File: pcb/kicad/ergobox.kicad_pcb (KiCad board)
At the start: 2 copper layers, 234.6 x 150.2 mm, 80 parts, among them SW1 SW_Push, SW10 Kailh, SW11 Kailh, SW12 Kailh, SW13 Kailh, SW14 Kailh, SW15 Kailh, SW16 Kailh, SW17 Kailh, SW18 Kailh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

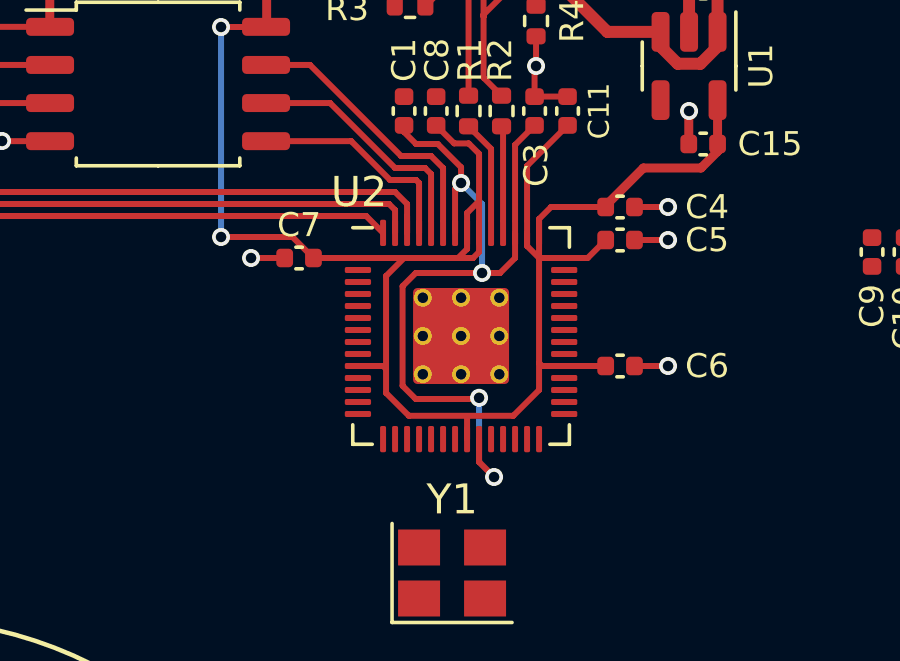
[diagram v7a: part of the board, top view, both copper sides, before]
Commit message: feat: adds +3V3 copper fill in RP2040 footprint
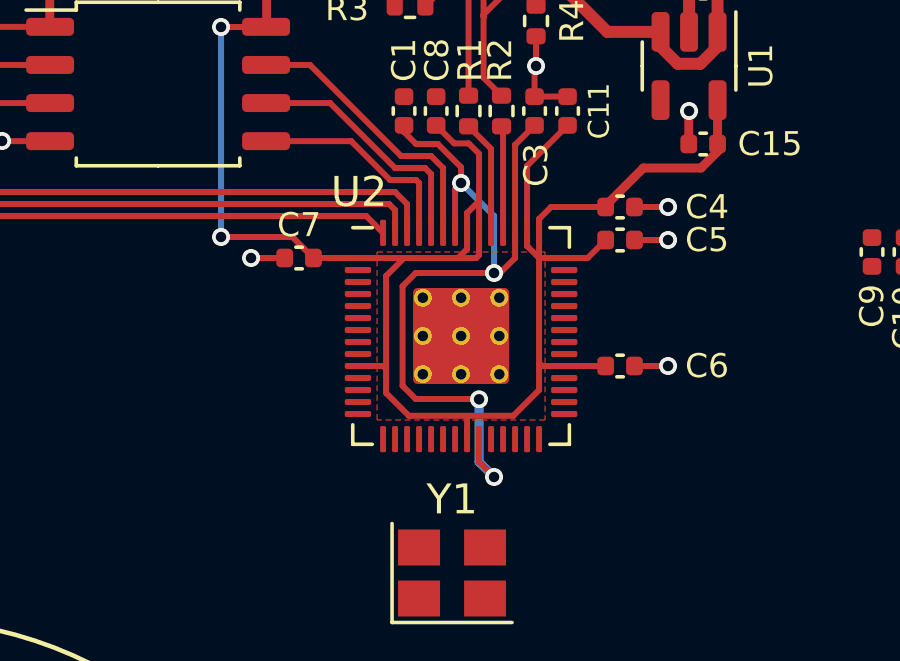
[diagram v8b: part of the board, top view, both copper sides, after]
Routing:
- added copper zone on F.Cu, net +3V3
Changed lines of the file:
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@@
   (segment (start 59.824314 27.2) (end 59.1 27.2) (width 0.2) (layer "F.Cu") (net 1))
   (segment (start 63.05 26.58) (end 62.4 27.23) (width 0.2) (layer "F.Cu") (net 1))
+  (segment (start 61.9 31.5) (end 62.4 31) (width 0.2) (layer "F.Cu") (net 1))
+  (segment (start 58.65 31.939379) (end 58.65 35.260621) (width 0.2) (layer "F.Cu") (net 1))
   (segment (start 60.6005 28.5) (end 60.6005 27.976186) (width 0.2) (layer "F.Cu") (net 1))
-  (segment (start 58.65 35.260621) (end 58.65 31.939379) (width 0.2) (layer "F.Cu") (net 1))
-  (segment (start 61.9 31.5) (end 61.3 31.5) (width 0.2) (layer "F.Cu") (net 1))
+  (segment (start 58.65 35.260621) (end 59.089379 35.7) (width 0.2) (layer "F.Cu") (net 1))
+  (segment (start 61.7 31.5) (end 61.9 31.5) (width 0.2) (layer "F.Cu") (net 1))
+  (segment (start 62.4 31) (end 62.4 30.1625) (width 0.2) (layer "F.Cu") (net 1))
   (segment (start 61.2 37.8) (end 61.7 38.3) (width 0.2) (layer "F.Cu") (net 1))
+  (segment (start 61.7 31.5) (end 59.089379 31.5) (width 0.2) (layer "F.Cu") (net 1))
   (segment (start 61.2 37.0375) (end 61.2 37.8) (width 0.2) (layer "F.Cu") (net 1))
-  (segment (start 62.4 31) (end 61.9 31.5) (width 0.2) (layer "F.Cu") (net 1))
+  (segment (start 59.089379 31.5) (end 58.65 31.939379) (width 0.2) (layer "F.Cu") (net 1))
   (segment (start 59.1 27.2) (end 58.7 26.8) (width 0.2) (layer "F.Cu") (net 1))
   (segment (start 60.6005 27.976186) (end 59.824314 27.2) (width 0.2) (layer "F.Cu") (net 1))
-  (segment (start 58.65 31.939379) (end 59.089379 31.5) (width 0.2) (layer "F.Cu") (net 1))
   (segment (start 62.4 27.23) (end 62.4 29.7625) (width 0.2) (layer "F.Cu") (net 1))
   (segment (start 58.7 26.8) (end 58.7 26.58) (width 0.2) (layer "F.Cu") (net 1))
+  (segment (start 59.089379 35.7) (end 61.2 35.7) (width 0.2) (layer "F.Cu") (net 1))
   (segment (start 60.4 30.1625) (end 60.4 28.7005) (width 0.2) (layer "F.Cu") (net 1))
-  (segment (start 61.2 35.7) (end 59.089379 35.7) (width 0.2) (layer "F.Cu") (net 1))
-  (segment (start 59.089379 35.7) (end 58.65 35.260621) (width 0.2) (layer "F.Cu") (net 1))
-  (segment (start 62.4 30.1625) (end 62.4 31) (width 0.2) (layer "F.Cu") (net 1))
-  (segment (start 59.089379 31.5) (end 61.3 31.5) (width 0.2) (layer "F.Cu") (net 1))
   (segment (start 60.4 28.7005) (end 60.6005 28.5) (width 0.2) (layer "F.Cu") (net 1))
-  (via (at 61.3 31.5) (size 0.6) (drill 0.35) (layers "F.Cu" "B.Cu") (net 1))
+  (via (at 61.7 31.5) (size 0.6) (drill 0.35) (layers "F.Cu" "B.Cu") (net 1))
   (via (at 60.6005 28.5) (size 0.6) (drill 0.35) (layers "F.Cu" "B.Cu") (net 1))
-  (via (at 61.2 35.66) (size 0.6) (drill 0.35) (layers "F.Cu" "B.Cu") (net 1))
+  (via (at 61.2 35.71) (size 0.6) (drill 0.35) (layers "F.Cu" "B.Cu") (net 1))
   (via (at 61.7 38.3) (size 0.6) (drill 0.35) (layers "F.Cu" "B.Cu") (net 1))
-  (segment (start 61.2 35.7) (end 61.2 37.8) (width 0.2) (layer "B.Cu") (net 1))
-  (segment (start 61.2 37.8) (end 61.7 38.3) (width 0.2) (layer "B.Cu") (net 1))
-  (segment (start 61.3 29.1995) (end 61.3 31.5) (width 0.2) (layer "B.Cu") (net 1))
-  (segment (start 60.6005 28.5) (end 61.3 29.1995) (width 0.2) (layer "B.Cu") (net 1))
+  (segment (start 61.7 31.5) (end 61.7 29.5995) (width 0.2) (layer "B.Cu") (net 1))
+  (segment (start 61.2 35.7) (end 61.2 37.8) (width 0.3) (layer "B.Cu") (net 1))
+  (segment (start 61.7 29.5995) (end 60.6005 28.5) (width 0.2) (layer "B.Cu") (net 1))
+  (segment (start 61.2 37.8) (end 61.7 38.3) (width 0.3) (layer "B.Cu") (net 1))
   (segment (start 66.38 29.3) (end 67.5 29.3) (width 0.2) (layer "F.Cu") (net 2))
   (segment (start 54.72 31) (end 53.6 31) (width 0.2) (layer "F.Cu") (net 2))
@@
   (via (at 67.3 22) (size 0.6) (drill 0.35) (layers "F.Cu" "B.Cu") (net 2))
   (via (at 68.2 26.1) (size 0.6) (drill 0.35) (layers "F.Cu" "B.Cu") (net 2))
+  (segment (start 61.2 30.1625) (end 61.2 30.9) (width 0.2) (layer "F.Cu") (net 3))
   (segment (start 64.82 31) (end 65.42 30.4) (width 0.2) (layer "F.Cu") (net 3))
   (segment (start 58.1 34.7) (end 58.1 35.5) (width 0.2) (layer "F.Cu") (net 3))
   (segment (start 61.2 27.525686) (end 60.854314 27.18) (width 0.2) (layer "F.Cu") (net 3))
-  (segment (start 61 31) (end 60.5 31) (width 0.2) (layer "F.Cu") (net 3))
+  (segment (start 60.5 31) (end 58.3 31) (width 0.2) (layer "F.Cu") (net 3))
   (segment (start 62.34 36.26) (end 63.2 35.4) (width 0.2) (layer "F.Cu") (net 3))
   (segment (start 54.98 30.3) (end 52.6 30.3) (width 0.2) (layer "F.Cu") (net 3))
@@
   (segment (start 57.1625 34.6) (end 58 34.6) (width 0.2) (layer "F.Cu") (net 3))
   (segment (start 60.8 37.0375) (end 60.8 36.3) (width 0.2) (layer "F.Cu") (net 3))
-  (segment (start 61.2 30.8) (end 61 31) (width 0.2) (layer "F.Cu") (net 3))
   (segment (start 62.8 30.1625) (end 62.8 30.6) (width 0.2) (layer "F.Cu") (net 3))
   (segment (start 54.12 23.275) (end 54.1 23.295) (width 0.3) (layer "F.Cu") (net 3))
@@
   (segment (start 55.68 31) (end 54.98 30.3) (width 0.2) (layer "F.Cu") (net 3))
   (segment (start 58.7 31) (end 58.1 31.6) (width 0.2) (layer "F.Cu") (net 3))
-  (segment (start 60.8 30.7) (end 60.5 31) (width 0.2) (layer "F.Cu") (net 3))
+  (segment (start 58.7 31) (end 58.3 31) (width 0.2) (layer "F.Cu") (net 3))
   (segment (start 61.2 30.1625) (end 61.2 29.1) (width 0.2) (layer "F.Cu") (net 3))
   (segment (start 69.15 27.45) (end 68.6 28) (width 0.3) (layer "F.Cu") (net 3))
@@
   (segment (start 54.12 21.5) (end 47.91 21.5) (width 0.3) (layer "F.Cu") (net 3))
   (segment (start 60.37 27.18) (end 59.77 26.58) (width 0.2) (layer "F.Cu") (net 3))
-  (segment (start 61.2 30.1625) (end 61.2 30.8) (width 0.2) (layer "F.Cu") (net 3))
   (segment (start 63.6 29.3) (end 65.42 29.3) (width 0.2) (layer "F.Cu") (net 3))
-  (segment (start 58.7 31) (end 57.1625 31) (width 0.2) (layer "F.Cu") (net 3))
   (segment (start 52.6 23.3) (end 54.095 23.3) (width 0.2) (layer "F.Cu") (net 3))
   (segment (start 64.0375 34.6) (end 63.3 34.6) (width 0.2) (layer "F.Cu") (net 3))
@@
   (segment (start 64.0375 34.6) (end 65.42 34.6) (width 0.2) (layer "F.Cu") (net 3))
   (segment (start 64.0375 31) (end 63.2 31) (width 0.2) (layer "F.Cu") (net 3))
-  (segment (start 60.5 31) (end 58.7 31) (width 0.2) (layer "F.Cu") (net 3))
   (segment (start 58.86 36.26) (end 62.34 36.26) (width 0.2) (layer "F.Cu") (net 3))
   (segment (start 66.677035 28) (end 65.42 29.257035) (width 0.3) (layer "F.Cu") (net 3))
+  (segment (start 58.3 31) (end 57.1625 31) (width 0.2) (layer "F.Cu") (net 3))
   (segment (start 63.2 35.4) (end 63.2 34.5) (width 0.2) (layer "F.Cu") (net 3))
+  (segment (start 60.8 30.7) (end 60.5 31) (width 0.2) (layer "F.Cu") (net 3))
   (segment (start 57.1625 31) (end 55.68 31) (width 0.2) (layer "F.Cu") (net 3))
   (segment (start 61.2 29.1) (end 61.2 27.525686) (width 0.2) (layer "F.Cu") (net 3))
@@
   (segment (start 62.8 30.6) (end 63.2 31) (width 0.2) (layer "F.Cu") (net 3))
   (segment (start 65.42 29.257035) (end 65.42 29.3) (width 0.3) (layer "F.Cu") (net 3))
+  (segment (start 61.2 30.9) (end 61.1 31) (width 0.2) (layer "F.Cu") (net 3))
   (segment (start 60.8 30.1625) (end 60.8 29.5) (width 0.2) (layer "F.Cu") (net 3))
   (segment (start 64.0375 31) (end 64.82 31) (width 0.2) (layer "F.Cu") (net 3))
@@
   (segment (start 63.2 29.7) (end 63.6 29.3) (width 0.2) (layer "F.Cu") (net 3))
   (segment (start 54.095 23.3) (end 54.1 23.295) (width 0.2) (layer "F.Cu") (net 3))
+  (segment (start 61.1 31) (end 60.5 31) (width 0.2) (layer "F.Cu") (net 3))
   (segment (start 60.8 29.5) (end 61.2 29.1) (width 0.2) (layer "F.Cu") (net 3))
   (via (at 52.6 23.3) (size 0.6) (drill 0.35) (layers "F.Cu" "B.Cu") (net 3))
@@
   (segment (start 44.835 24.565) (end 46.9 24.565) (width 0.2) (layer "F.Cu") (net 66))
   (segment (start 44 25.4) (end 44.835 24.565) (width 0.2) (layer "F.Cu") (net 66))
+  (zone (net 3) (net_name "+3V3") (layer "F.Cu") (hatch edge 0.508)
+    (connect_pads yes (clearance 0.15))
+    (min_thickness 0.15) (filled_areas_thickness no)
+    (fill yes (thermal_gap 0.508) (thermal_bridge_width 0.508))
+    (polygon
+      (pts
+        (xy 63.4 36.4)
+        (xy 57.8 36.4)
+        (xy 57.8 30.8)
+        (xy 63.4 30.8)
+      )
+    )
+  )
   (zone (net 2) (net_name "GND") (layer "F.Cu") (name "GND") (hatch edge 0.508)
     (connect_pads (clearance 0.2))
